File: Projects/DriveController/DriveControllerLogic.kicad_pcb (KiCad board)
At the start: 2 copper layers, 70 parts, among them J1 HPCE_40-24, J2 ISP_Header, Q1 PSMN1R0, Q2 PSMN1R0, Q3 PSMN1R0, Q4 PSMN1R0, Q5 PSMN1R0, Q6 PSMN1R0, Q7 PSMN1R0, Q8 BC817-40, U1 ATMega32M1, U2 MCP2562, U3 ATA6844, U4 ACS710

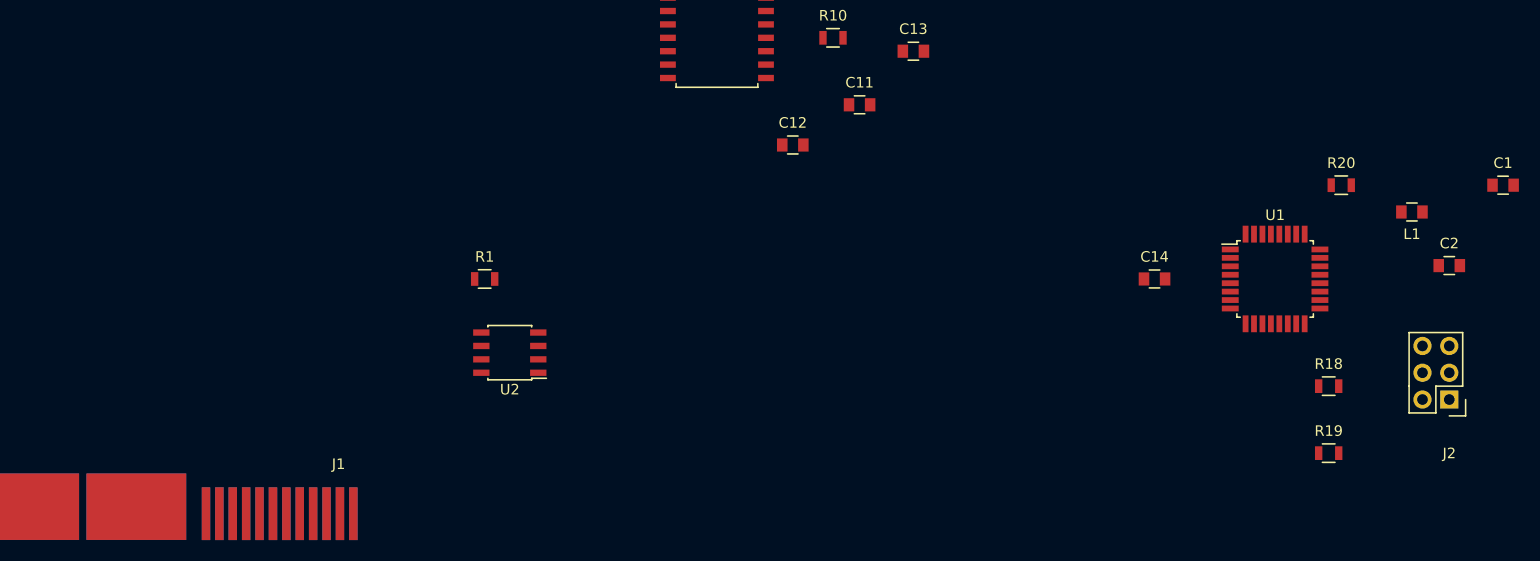
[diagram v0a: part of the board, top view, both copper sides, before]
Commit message: More routing
Might start traces over. :page_facing_up:
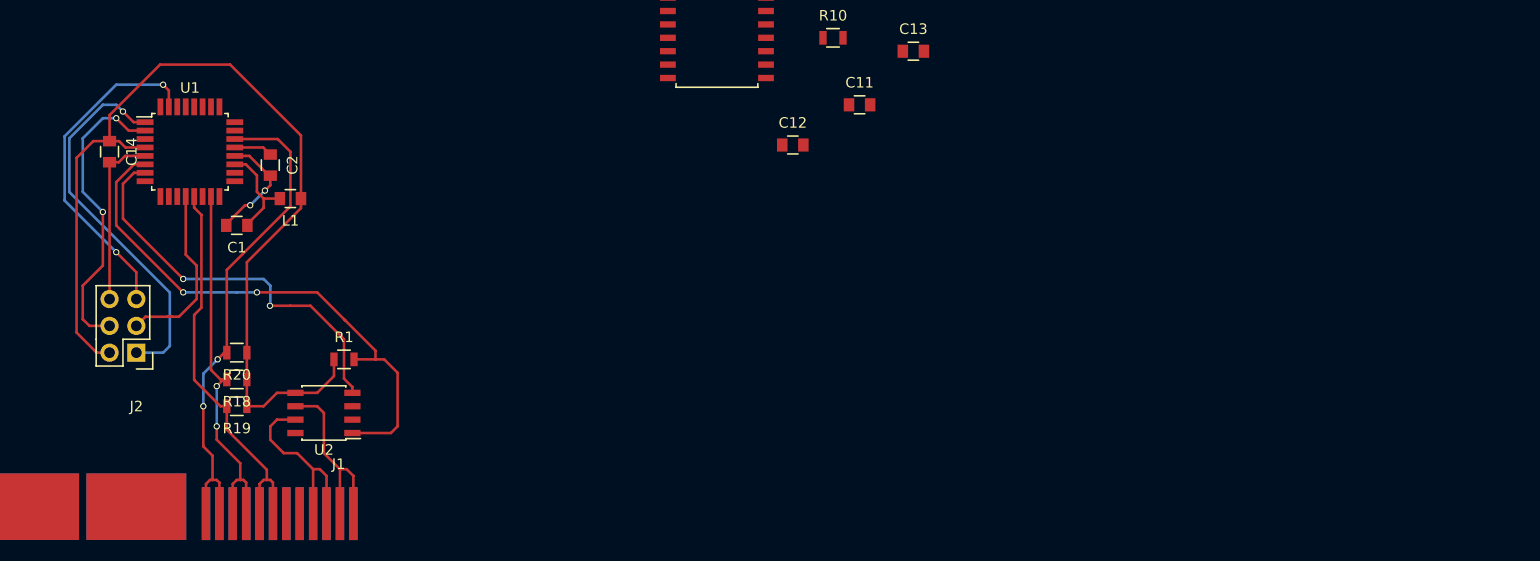
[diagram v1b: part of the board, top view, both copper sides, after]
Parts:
- Q1, Q2, Q3, Q4, Q5, Q6, Q7: footprint TO_SOT_Packages_SMD:SOT-669_LFPAK_ThermalVias-1 -> USSTPARTS:SOT-669_LFPAK_POWERSO8
- moved J2 124.5 mm to (142.2, 131.4)
- moved C1 120.1 mm to (151.8, 119.4), turned to 180 degrees
- moved C2 112.2 mm to (154.9, 113.7), turned to 270 degrees
- moved L1 106.3 mm to (156.8, 116.8)
- moved R20 105.9 mm to (151.8, 131.4), turned to 180 degrees
- moved R19 103.6 mm to (151.8, 136.5), turned to 180 degrees
- moved U1 103.6 mm to (147.3, 112.4)
- moved R18 103.5 mm to (151.8, 134.0), turned to 180 degrees
- moved C14 99.8 mm to (139.7, 112.4), turned to 270 degrees
- moved U2 18.5 mm to (160.0, 137.2)
- moved R1 15.4 mm to (161.9, 132.1)
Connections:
- Q1 pad 5: (no net) -> /DriveControllerPower/PBAT
- Q2 pad 5: (no net) -> /DriveControllerPower/PBAT
- Q3 pad 5: (no net) -> /DriveControllerPower/PBAT
- Q4 pad 5: (no net) -> /DriveControllerPower/U
- Q5 pad 5: (no net) -> /DriveControllerPower/V
- Q6 pad 5: (no net) -> /DriveControllerPower/W
- Q7 pad 5: (no net) -> /DriveControllerPower/PBAT
- R18 pad 2: /HA2 -> /DriveControllerPower/H2
- R19 pad 2: /HA3 -> /DriveControllerPower/H3
- R20 pad 2: /HA1 -> /DriveControllerPower/H1
- U1 pad 13: /HA3 -> /DriveControllerPower/H3
- U1 pad 15: /HA2 -> /DriveControllerPower/H2
- U1 pad 22: /HA1 -> /DriveControllerPower/H1
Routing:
- net /5V0: track 0.00 -> 92.1 mm
- net /TXCAN: track 0.00 -> 52.3 mm, vias 0 -> 2
- net /DriveControllerPower/H1: track 0.00 -> 48.1 mm, vias 0 -> 2
- net /RXCAN: track 0.00 -> 38.1 mm, vias 0 -> 2
- net /DriveControllerPower/H3: track 0.00 -> 37.9 mm
- net /DriveControllerPower/H2: track 0.00 -> 36.3 mm, vias 0 -> 2
- net /MISO: track 0.00 -> 36.2 mm, vias 0 -> 1
- net /NRESET: track 0.00 -> 31.9 mm, vias 0 -> 2
- net /MOSI: track 0.00 -> 28.7 mm, vias 0 -> 2
- net /LGND: track 0.00 -> 27.5 mm, vias 0 -> 2
- net /CANH: track 0.00 -> 18.5 mm
- net /CANL: track 0.00 -> 18.3 mm
- net /SCK: track 0.00 -> 17.4 mm
- net Net-(C1-Pad1): track 0.00 -> 9.71 mm
- net Net-(C2-Pad1): track 0.00 -> 3.65 mm

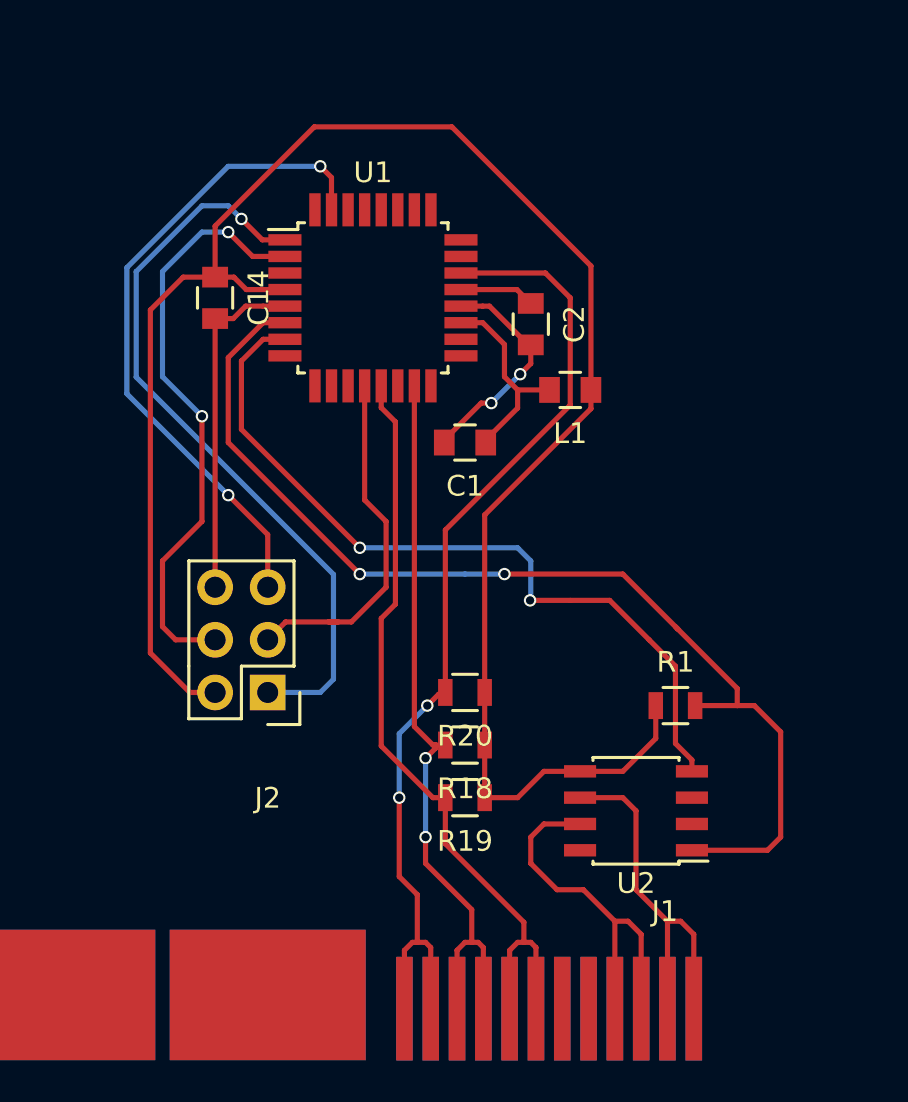
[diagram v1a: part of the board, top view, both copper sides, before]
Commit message: Redoing traces
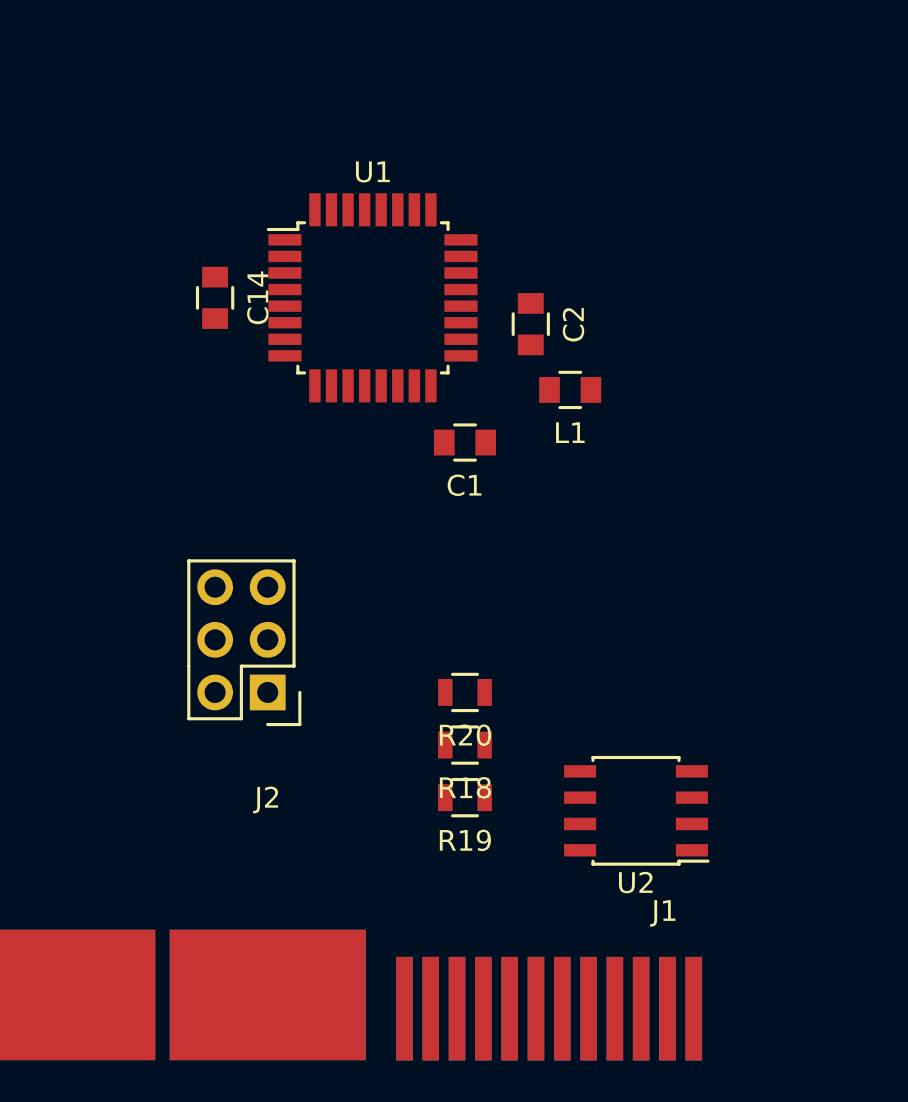
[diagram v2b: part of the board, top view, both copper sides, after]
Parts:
- removed R1: 10k, Resistors_SMD:R_0805
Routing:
- net /5V0: track 92.1 -> 0.00 mm
- net /TXCAN: track 52.3 -> 0.00 mm, vias 2 -> 0
- net /DriveControllerPower/H1: track 48.1 -> 0.00 mm, vias 2 -> 0
- net /RXCAN: track 38.1 -> 0.00 mm, vias 2 -> 0
- net /DriveControllerPower/H3: track 37.9 -> 0.00 mm
- net /DriveControllerPower/H2: track 36.3 -> 0.00 mm, vias 2 -> 0
- net /MISO: track 36.2 -> 0.00 mm, vias 1 -> 0
- net /NRESET: track 31.9 -> 0.00 mm, vias 2 -> 0
- net /MOSI: track 28.7 -> 0.00 mm, vias 2 -> 0
- net /LGND: track 27.5 -> 0.00 mm, vias 2 -> 0
- net /CANH: track 18.5 -> 0.00 mm
- net /CANL: track 18.3 -> 0.00 mm
- net /SCK: track 17.4 -> 0.00 mm
- net Net-(C1-Pad1): track 9.71 -> 0.00 mm
- net Net-(C2-Pad1): track 3.65 -> 0.00 mm

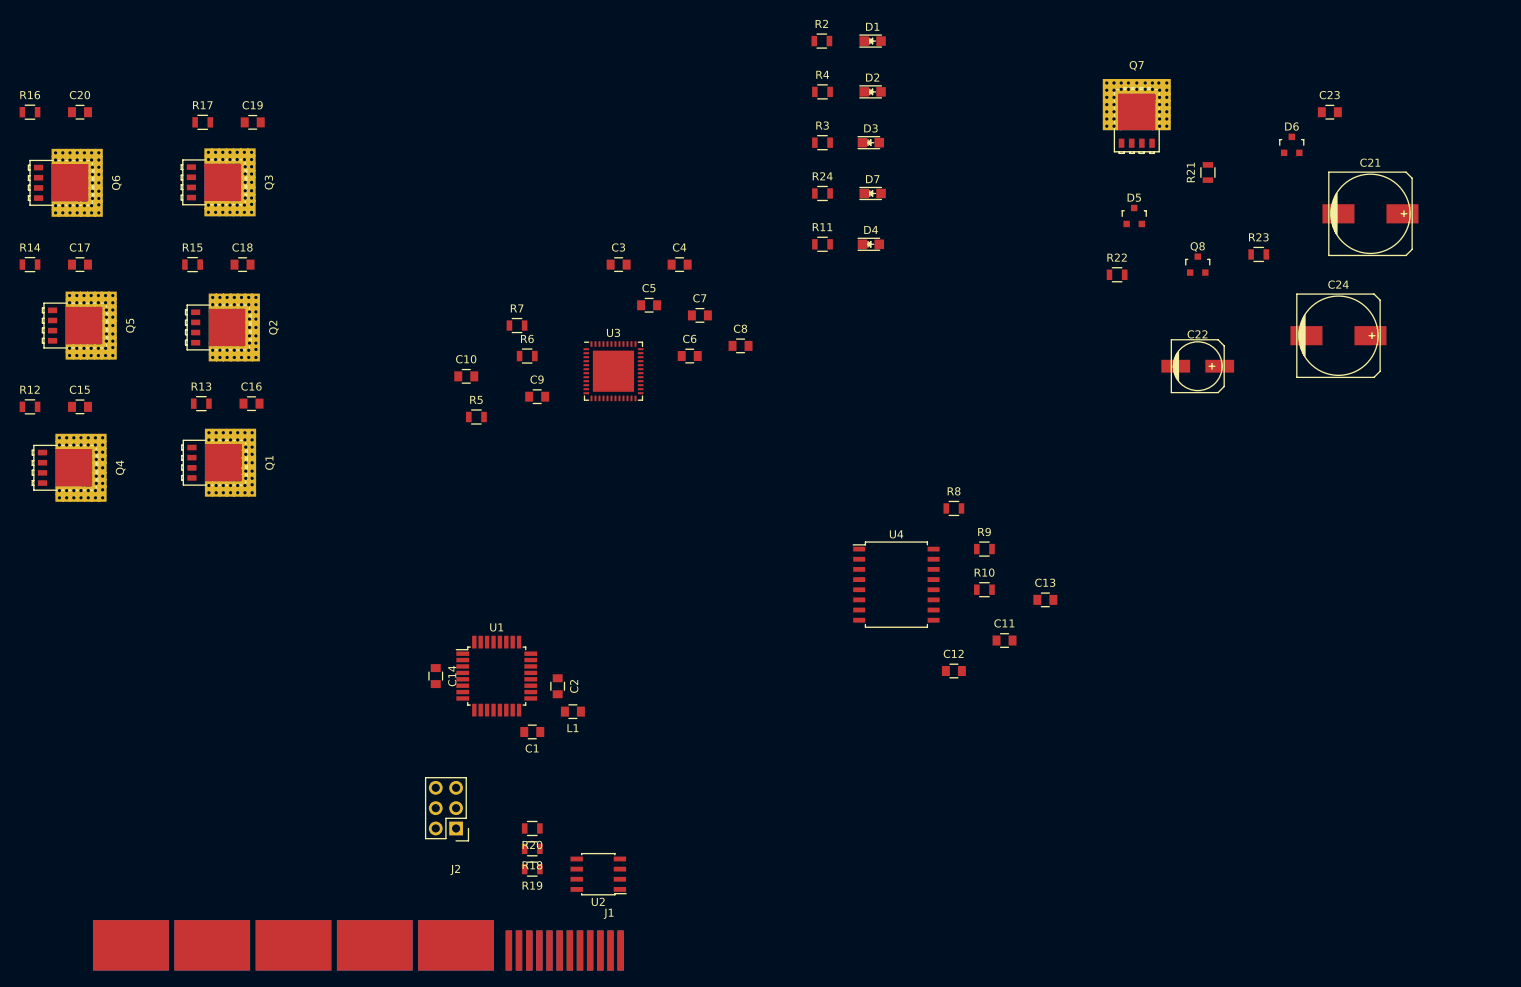
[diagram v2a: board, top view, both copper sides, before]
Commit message: Redone some routing - nearly finished!
There's a lot of room for improvement on the digital side.
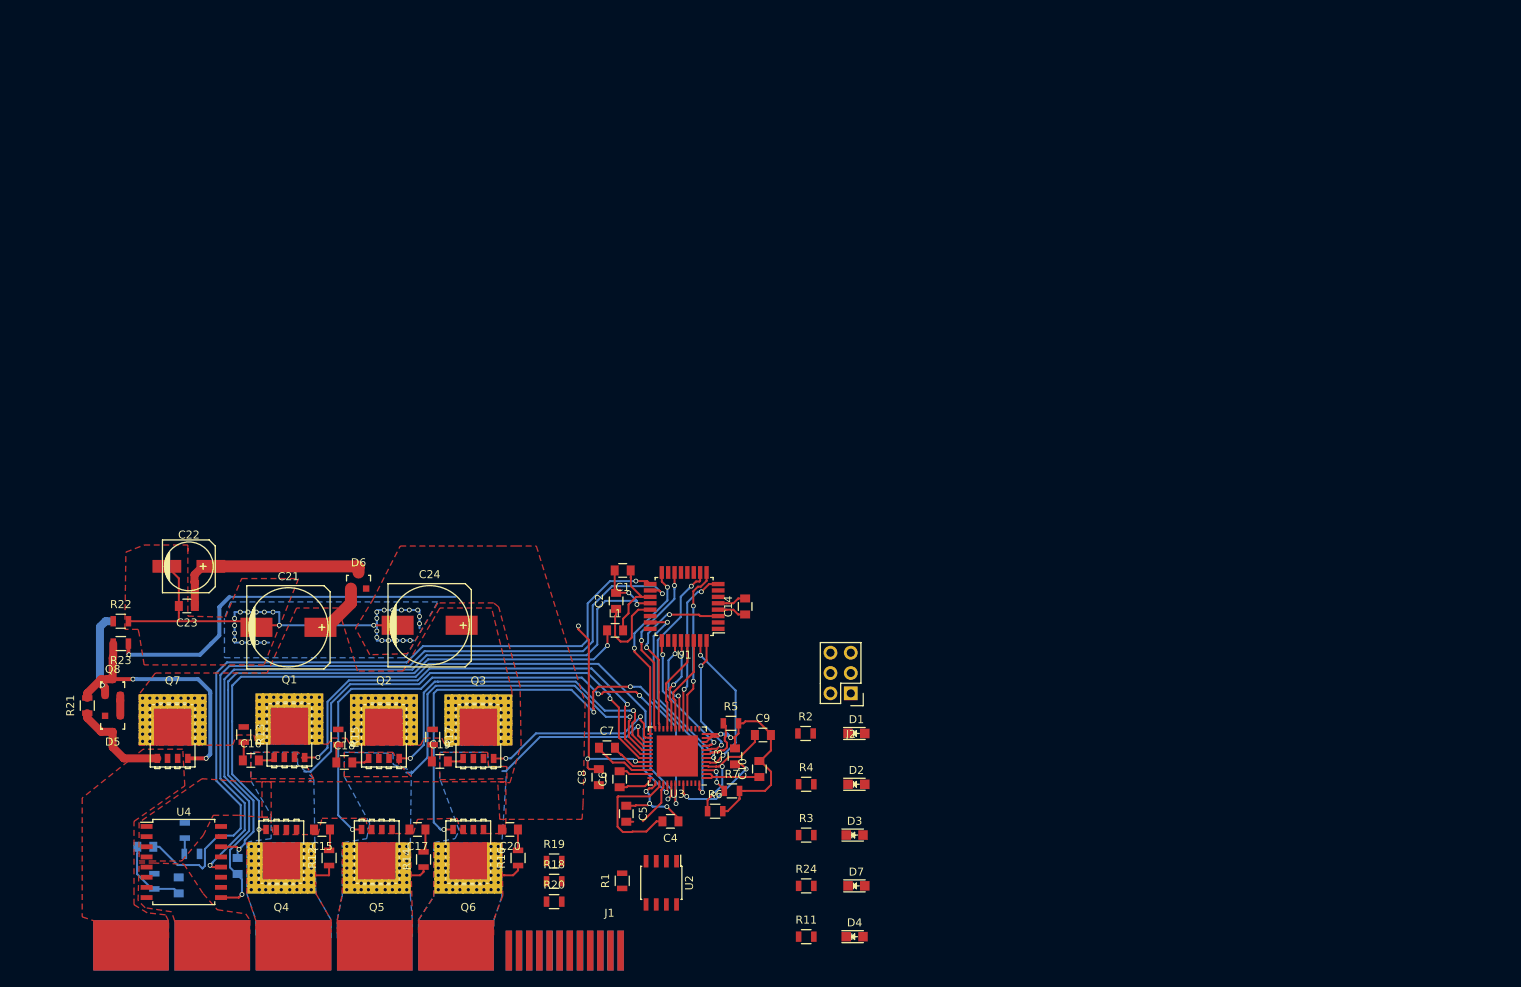
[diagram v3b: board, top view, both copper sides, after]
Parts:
- added R1: 10k, Resistors_SMD:R_0805, F.Cu at (163.0, 138.0)
- C11, C12, C13, R10, R8, R9: moved to B.Cu
- moved C23 155.6 mm to (108.6, 103.6), turned to 180 degrees
- moved R21 155.1 mm to (96.1, 116.1)
- moved R23 150.3 mm to (100.3, 108.3), turned to 180 degrees
- moved Q8 145.6 mm to (99.3, 113.8)
- moved C21 144.8 mm to (121.3, 106.3)
- moved Q7 143.0 mm to (106.8, 119.9)
- moved D5 142.6 mm to (99.3, 118.4), turned to 180 degrees
- moved R22 131.9 mm to (100.3, 105.5)
- moved D6 128.7 mm to (130.0, 100.5)
- moved C22 128.6 mm to (108.8, 98.7)
- moved C24 119.2 mm to (138.9, 106.0)
- moved R16 111.4 mm to (150.0, 135.1), turned to 90 degrees
- moved C11 110.5 mm to (103.4, 133.7), turned to 180 degrees
- moved R10 110.0 mm to (104.5, 138.0), turned to 270 degrees
- moved C13 106.3 mm to (114.9, 136.1), turned to 270 degrees
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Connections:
- J1 pad 41: /DriveControllerPower/H1 -> /HA1
- J1 pad 42: /DriveControllerPower/H1 -> /HA1
- J1 pad 43: /DriveControllerPower/H2 -> /HA2
- J1 pad 44: /DriveControllerPower/H2 -> /HA2
- J1 pad 45: /DriveControllerPower/H3 -> /HA3
- J1 pad 46: /DriveControllerPower/H3 -> /HA3
- R18 pad 2: /DriveControllerPower/H2 -> /HA2
- R19 pad 2: /DriveControllerPower/H3 -> /HA1
- R20 pad 2: /DriveControllerPower/H1 -> /HA3
- U1 pad 13: /DriveControllerPower/H3 -> /HA1
- U1 pad 15: /DriveControllerPower/H2 -> /HA2
- U1 pad 22: /DriveControllerPower/H1 -> /HA3
- U3 pad 13: Net-(U3-Pad13) -> (no net)
- U3 pad 15: Net-(U3-Pad15) -> (no net)
- U3 pad 22: Net-(U3-Pad22) -> (no net)
- U4 pad 13: /I_OK -> (no net)
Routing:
- net /LGND: track 0.00 -> 143.7 mm, vias 0 -> 5
- net /ISENSEN: track 0.00 -> 97.9 mm, vias 0 -> 1
- net /5V0: track 0.00 -> 94.1 mm, vias 0 -> 4
- net /ISENSEP: track 0.00 -> 92.9 mm, vias 0 -> 2
- net /DriveControllerPower/L1: track 0.00 -> 88.2 mm, vias 0 -> 2
- net /DriveControllerPower/PGND: track 0.00 -> 86.0 mm, vias 0 -> 34
- net /DriveControllerPower/L2: track 0.00 -> 75.4 mm, vias 0 -> 4
- net /DriveControllerPower/CPOUT: track 0.00 -> 75.1 mm, vias 0 -> 4
- net /DriveControllerPower/L3: track 0.00 -> 68.1 mm, vias 0 -> 4
- net /DriveControllerPower/U: track 0.00 -> 64.2 mm, vias 0 -> 1
- net /DriveControllerPower/H1: track 0.00 -> 58.5 mm, vias 0 -> 2
- net /DriveControllerPower/V: track 0.00 -> 49.7 mm, vias 0 -> 1
- net /DriveControllerPower/H2: track 0.00 -> 44.6 mm, vias 0 -> 2
- net Net-(Q7-Pad1): track 0.00 -> 32.7 mm, vias 0 -> 2
- net /WD: track 0.00 -> 29.7 mm, vias 0 -> 2
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- added copper zone on F.Cu, net /DriveControllerPower/PBAT
- added copper zone on B.Cu, net /DriveControllerPower/PGND
- added copper zone on F.Cu, net /DriveControllerPower/PGND
- added copper zone on F.Cu, net /DriveControllerPower/POUT
- added copper zone on B.Cu, net /DriveControllerPower/U
- added copper zone on F.Cu, net /DriveControllerPower/U
- added copper zone on B.Cu, net /DriveControllerPower/V
- added copper zone on F.Cu, net /DriveControllerPower/V
- added copper zone on F.Cu, net /DriveControllerPower/VSUPPLY
- added copper zone on B.Cu, net /DriveControllerPower/W
- added copper zone on F.Cu, net /DriveControllerPower/W
